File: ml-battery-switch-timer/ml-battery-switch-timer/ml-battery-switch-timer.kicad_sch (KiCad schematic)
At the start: 18 parts, among them J1 XT60 IPW to ML Power, U1 TLC555 CMOS, U2 TLC555 CMOS, U3 TLC555 CMOS, U4 Pololu Switch (ML Battery Con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

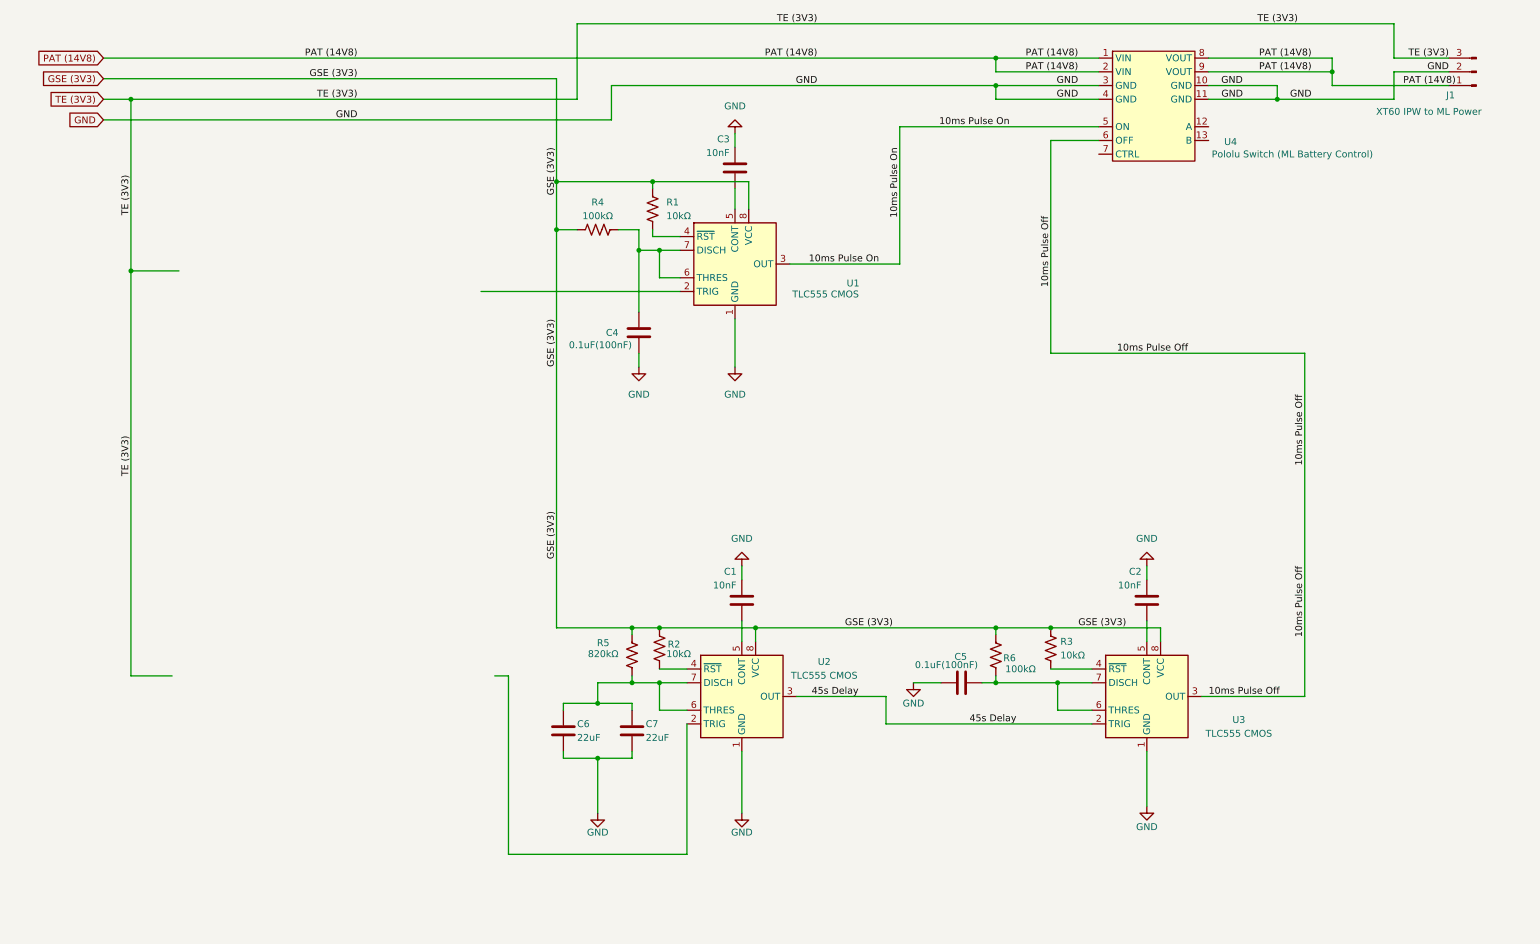
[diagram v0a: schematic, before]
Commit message: Added updated ML power logic timer
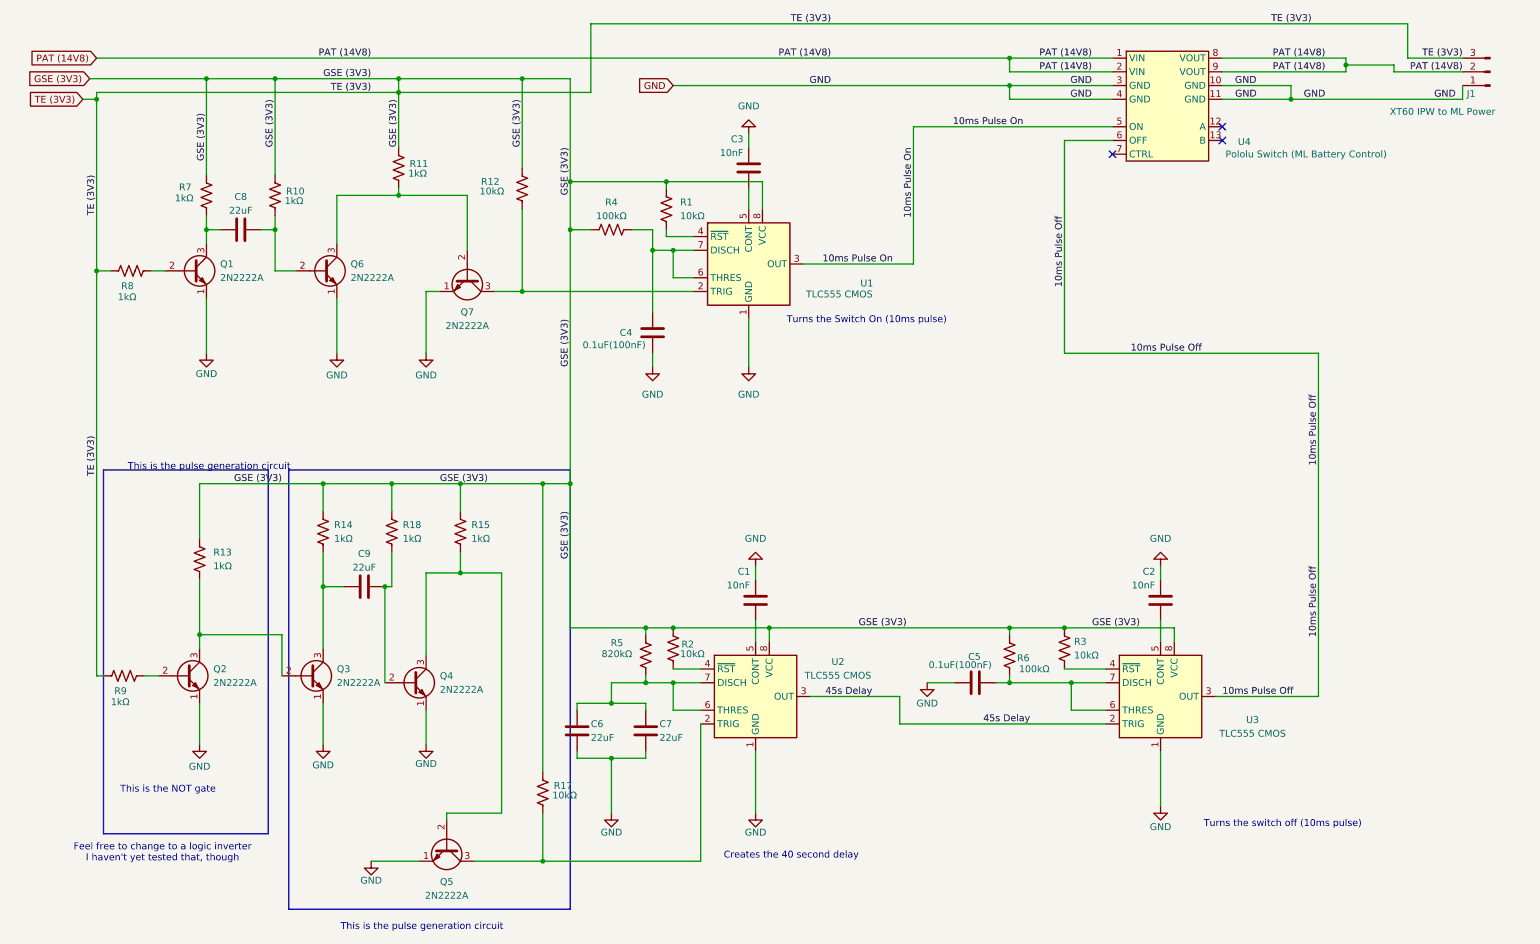
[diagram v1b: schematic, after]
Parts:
- added C8, C9: 22uF, symbol Device:C
- added Q1, Q2, Q3, Q4, Q5, Q6, Q7: 2N2222A, symbol RockSat:2N2222A
- added R10, R11, R13, R14, R15, R18, R7, R8, R9: 1kΩ, symbol Device:R_US
- added R12, R17: 10kΩ, symbol Device:R_US
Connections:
- net TE (3V3) is gone; now on net GSE (3V3): J1.3 (Pin_3)
- net GND: now also J1.1 (Pin_1), Q1.1 (E), Q2.1 (E), Q3.1 (E), Q4.1 (E), Q5.1 (E), Q6.1 (E), Q7.1 (E); no longer J1.2 (Pin_2)
- net GSE (3V3): now also R10.1, R11.1, R12.1, R13.1, R14.1, R15.1, R17.1, R18.1, R7.1, R8.1, R9.1
- net PAT (14V8): now also J1.2 (Pin_2); no longer J1.1 (Pin_1)
- net at U2.2 (TRIG): now also Q5.3 (C), R17.2
- net at U1.2 (TRIG): now also Q7.3 (C), R12.2
- new net: C8.2, Q6.2 (B), R10.2
- new net: Q6.3 (C), Q7.2 (B), R11.2
- new net: C9.1, Q3.3 (C), R14.2
- new net: C9.2, Q4.2 (B), R18.2
- new net: Q2.3 (C), Q3.2 (B), R13.2
- new net: Q2.2 (B), R9.2
- new net: C8.1, Q1.3 (C), R7.2
- new net: Q4.3 (C), Q5.2 (B), R15.2
- new net: Q1.2 (B), R8.2
- no-connect marks 0 -> 3
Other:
- note added: "Creates the 40 second delay"
- note added: "Feel free to change to a logic inverter"
- note added: "I haven't yet tested that, though"
- note added: "This is the NOT gate"
- note added: "This is the pulse generation circuit"
- note added: "Turns the Switch On (10ms pulse)"
- note added: "Turns the switch off (10ms pulse)"
- company: (none) -> Mark Fullton and Aidan Schafer
- title: (none) -> Machine Learning Power Logic
- moved on the sheet: C1, C2, C3, C4, C5, C6, C7, J1, R1, R2, R3, R4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
